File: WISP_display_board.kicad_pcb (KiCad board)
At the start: 2 copper layers, 261 x 160 mm, 109 parts, among them J1 Conn_01x09_Socket, U1 74HC595, U2 74HC595, U3 74HC595, U4 74HC595, U6 74HC595, U7 74HC595, U8 74HC595, U9 74HC595

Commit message: Full 15 rough draft
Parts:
- added Brd2: SSD1306, ssd1306_custom:128x64OLED, F.Cu at (-0.05, 53.3)
- added Brd3: SSD1306, ssd1306_custom:128x64OLED, F.Cu at (-0.05, 81.7)
- added Brd4: SSD1306, ssd1306_custom:128x64OLED, F.Cu at (-0.05, 110.2)
- added Brd5: SSD1306, ssd1306_custom:128x64OLED, F.Cu at (-0.05, 138.6)
- added Brd6: SSD1306, ssd1306_custom:128x64OLED, F.Cu at (28.5, 53.3)
- added Brd7: SSD1306, ssd1306_custom:128x64OLED, F.Cu at (28.5, 81.7)
- added Brd8: SSD1306, ssd1306_custom:128x64OLED, F.Cu at (28.5, 110.2)
- added J1: Conn_01x10_Socket, Connector_PinHeader_2.54mm:PinHeader_1x10_P2.54mm_Vertical, F.Cu at (45.4, 57.0)
- added R61: 4.7k, Resistor_SMD:R_0805_2012Metric_Pad1.20x1.40mm_HandSolder, F.Cu at (59.5, 62.1)
- added R62: 4.7k, Resistor_SMD:R_0805_2012Metric_Pad1.20x1.40mm_HandSolder, F.Cu at (59.5, 65.1)
- added R63: 4.7k, Resistor_SMD:R_0805_2012Metric_Pad1.20x1.40mm_HandSolder, F.Cu at (59.5, 68.0)
- added R64: 4.7k, Resistor_SMD:R_0805_2012Metric_Pad1.20x1.40mm_HandSolder, F.Cu at (59.5, 71.0)
- added R65: 4.7k, Resistor_SMD:R_0805_2012Metric_Pad1.20x1.40mm_HandSolder, F.Cu at (59.5, 73.9)
- added R66: 4.7k, Resistor_SMD:R_0805_2012Metric_Pad1.20x1.40mm_HandSolder, F.Cu at (59.5, 76.9)
- added R67: 4.7k, Resistor_SMD:R_0805_2012Metric_Pad1.20x1.40mm_HandSolder, F.Cu at (59.5, 79.8)
- added R68: 4.7k, Resistor_SMD:R_0805_2012Metric_Pad1.20x1.40mm_HandSolder, F.Cu at (64.3, 56.2)
- added R69: 4.7k, Resistor_SMD:R_0805_2012Metric_Pad1.20x1.40mm_HandSolder, F.Cu at (64.3, 59.2)
- added R70: 4.7k, Resistor_SMD:R_0805_2012Metric_Pad1.20x1.40mm_HandSolder, F.Cu at (64.3, 62.1)
- added R71: 4.7k, Resistor_SMD:R_0805_2012Metric_Pad1.20x1.40mm_HandSolder, F.Cu at (64.3, 65.1)
- added R72: 4.7k, Resistor_SMD:R_0805_2012Metric_Pad1.20x1.40mm_HandSolder, F.Cu at (64.3, 68.0)
- added R73: 4.7k, Resistor_SMD:R_0805_2012Metric_Pad1.20x1.40mm_HandSolder, F.Cu at (64.3, 71.0)
- added R74: 4.7k, Resistor_SMD:R_0805_2012Metric_Pad1.20x1.40mm_HandSolder, F.Cu at (64.3, 73.9)
- added R75: 4.7k, Resistor_SMD:R_0805_2012Metric_Pad1.20x1.40mm_HandSolder, F.Cu at (64.3, 76.9)
- added R76: 4.7k, Resistor_SMD:R_0805_2012Metric_Pad1.20x1.40mm_HandSolder, F.Cu at (64.3, 79.8)
- added U5: TCA9548APWR, Package_SO:TSSOP-24_4.4x7.8mm_P0.65mm, F.Cu at (71.5, 86.9)
- moved R23 197.5 mm to (50.0, 76.9), turned to 0 degrees
- moved R22 193.1 mm to (50.0, 73.9), turned to 0 degrees
- moved D10 192.1 mm to (49.0, 85.4)
- moved D11 192.1 mm to (53.0, 85.4)
- moved D9 192.1 mm to (45.0, 85.4)
- moved D12 192.1 mm to (56.9, 85.4)
- moved R21 188.9 mm to (50.0, 71.0), turned to 0 degrees
- moved R20 184.7 mm to (50.0, 68.0), turned to 0 degrees
- moved R19 180.6 mm to (50.0, 65.1), turned to 0 degrees
- moved R18 176.4 mm to (50.0, 62.1), turned to 0 degrees
- moved R17 172.2 mm to (50.0, 59.2), turned to 0 degrees
- moved R16 168.1 mm to (50.0, 56.2), turned to 0 degrees
- moved C7 155.3 mm to (78.1, 85.9)
- moved C3 153.3 mm to (78.1, 83.4)
- moved D29 152.4 mm to (53.0, 91.7)
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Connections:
- Brd1 pad 3: /I2C1_SCL -> /SC0
- Brd1 pad 4: /I2C1_SDA -> /SD0

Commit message: V1 routing
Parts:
- removed the Brd2 at (-0.05, 53.3)
- removed the Brd2 at (159.6, 147.7)
- removed C6, C7, C8: 0.1uF, Capacitor_SMD:C_0603_1608Metric_Pad1.08x0.95mm_HandSolder
- removed D21, D22, D23, D24, D25, D26, D27, D28, D29, D30: LED_Dual_AAKK, LED_SMD:LED_Kingbright_KPBD-3224
- removed the J1 at (101.2, 140.4)
- removed the J1 at (45.4, 57.0)
- removed R57, R58, R59, R60: 750, Resistor_SMD:R_0805_2012Metric_Pad1.20x1.40mm_HandSolder
- removed R61, R62, R63, R64, R65, R66, R67, R68, R69, R70, R71, R72, R73, R74, R75, R76: 4.7k, Resistor_SMD:R_0805_2012Metric_Pad1.20x1.40mm_HandSolder
- removed the U2 at (122.0, 183.9)
- removed the U3 at (49.5, 47.6)
- removed the U5 at (71.5, 86.9)
- removed U8: 74HC595, Package_SO:SOIC-16W_7.5x12.8mm_P1.27mm
- added Brd2: SSD1306, ssd1306_custom:128x64OLED, F.Cu at (339.0, 141.0)
- added J1: Conn_01x10_Socket, Connector_JST:JST_XH_B10B-XH-A_1x10_P2.50mm_Vertical, F.Cu at (147.2, 203.0)
- added U1: TCA9548APWR, Package_SO:TSSOP-24_4.4x7.8mm_P0.65mm, F.Cu at (158.1, 166.0)
- R17, R18, R19, R20, R21, R22, R23, R24, R41, R42, R43, R44, R45, R46, R47, R48: value 750 -> 4.7k
- moved R18 306.9 mm to (350.0, 126.9), turned to 180 degrees
- moved U4 303.0 mm to (325.9, 197.3), turned to 180 degrees
- moved R16 301.4 mm to (350.5, 80.0)
- moved R22 300.2 mm to (345.5, 126.9)
- moved D11 281.7 mm to (324.0, 162.0), turned to -90 degrees
- moved D12 279.9 mm to (323.9, 169.2), turned to -90 degrees
- moved R53 276.9 mm to (295.5, 201.9)
- moved R54 274.0 mm to (295.5, 199.0)
- moved R55 271.3 mm to (295.5, 196.1)
- moved C3 269.4 mm to (326.1, 188.4), turned to 180 degrees
- moved R56 268.6 mm to (295.5, 193.1)
- moved R52 260.5 mm to (274.5, 202.1), turned to 180 degrees
- moved R50 260.4 mm to (274.5, 196.1), turned to 180 degrees
- moved R51 260.4 mm to (274.5, 199.0), turned to 180 degrees
- moved Brd4 254.0 mm to (253.2, 91.2)
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- renumbered U6 to U2, U7 to U3, U9 to U5, U1 to U6
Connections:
- R10 pad 1: /LED6_G -> /LED5_R
- R10 pad 2: Net-(D6-A1) -> Net-(D5-A2)
- R11 pad 1: /LED6_R -> /LED6_G
- R11 pad 2: Net-(D6-A2) -> Net-(D6-A1)
- R12 pad 1: /LED7_G -> /LED6_R
- R12 pad 2: Net-(D7-A1) -> Net-(D6-A2)
- R13 pad 1: /LED7_R -> /LED7_G
- R13 pad 2: Net-(D7-A2) -> Net-(D7-A1)
- R14 pad 1: /LED8_G -> /LED7_R
- R14 pad 2: Net-(D8-A1) -> Net-(D7-A2)
- R15 pad 1: /LED8_R -> /LED8_G
- R15 pad 2: Net-(D8-A2) -> Net-(D8-A1)
- R16 pad 1: /LED9_G -> /LED8_R
- R16 pad 2: Net-(D9-A1) -> Net-(D8-A2)
- R17 pad 1: /LED9_R -> /SD0
- R17 pad 2: Net-(D9-A2) -> +3.3V
- R18 pad 1: /LED10_G -> /SD1
- R18 pad 2: Net-(D10-A1) -> +3.3V
- R19 pad 1: /LED10_R -> /SD2
- R19 pad 2: Net-(D10-A2) -> +3.3V
- R2 pad 1: /LED2_G -> /LED1_R
- R2 pad 2: Net-(D2-A1) -> Net-(D1-A2)
- R20 pad 1: /LED11_G -> /SD3
- R20 pad 2: Net-(D11-A1) -> +3.3V
- R21 pad 1: /LED11_R -> +3.3V
- R21 pad 2: Net-(D11-A2) -> /SC0
- R22 pad 1: /LED12_G -> +3.3V
- R22 pad 2: Net-(D12-A1) -> /SC1
- R23 pad 1: /LED12_R -> +3.3V
- R23 pad 2: Net-(D12-A2) -> /SC2
- R24 pad 1: /LED13_G -> +3.3V
- R24 pad 2: Net-(D13-A1) -> /SC3
- R25 pad 1: /LED13_R -> /LED9_G
- R25 pad 2: Net-(D13-A2) -> Net-(D9-A1)
- R26 pad 1: /LED14_G -> /LED9_R
- R26 pad 2: Net-(D14-A1) -> Net-(D9-A2)
- R27 pad 1: /LED14_R -> /LED10_G
- R27 pad 2: Net-(D14-A2) -> Net-(D10-A1)
- R28 pad 1: /LED15_G -> /LED10_R
- R28 pad 2: Net-(D15-A1) -> Net-(D10-A2)
- R29 pad 1: /LED15_R -> /LED11_G
- R29 pad 2: Net-(D15-A2) -> Net-(D11-A1)
- R3 pad 1: /LED2_R -> /LED2_G
- R3 pad 2: Net-(D2-A2) -> Net-(D2-A1)
- R30 pad 1: /LED16_G -> /LED11_R
- R30 pad 2: Net-(D16-A1) -> Net-(D11-A2)
- R31 pad 1: /LED16_R -> /LED12_G
- R31 pad 2: Net-(D16-A2) -> Net-(D12-A1)
- R32 pad 1: /LED1_R -> /LED12_R
- R32 pad 2: Net-(D1-A2) -> Net-(D12-A2)
- R33 pad 1: /LED17_G -> /LED13_G
- R33 pad 2: Net-(D17-A1) -> Net-(D13-A1)
- R34 pad 1: /LED17_R -> /LED13_R
- R34 pad 2: Net-(D17-A2) -> Net-(D13-A2)
- R35 pad 1: /LED18_G -> /LED14_G
- R35 pad 2: Net-(D18-A1) -> Net-(D14-A1)
- R36 pad 1: /LED18_R -> /LED14_R
- R36 pad 2: Net-(D18-A2) -> Net-(D14-A2)
- R37 pad 1: /LED19_G -> /LED15_G
- R37 pad 2: Net-(D19-A1) -> Net-(D15-A1)
- R38 pad 1: /LED19_R -> /LED15_R
- R38 pad 2: Net-(D19-A2) -> Net-(D15-A2)
- R39 pad 1: /LED20_G -> /LED16_G
- R39 pad 2: Net-(D20-A1) -> Net-(D16-A1)
- R4 pad 1: /LED3_G -> /LED2_R
- R4 pad 2: Net-(D3-A1) -> Net-(D2-A2)
- R40 pad 1: /LED20_R -> /LED16_R
- R40 pad 2: Net-(D20-A2) -> Net-(D16-A2)
- R41 pad 1: /LED21_G -> /SD4
- R41 pad 2: Net-(D21-A1) -> +3.3V
- R42 pad 1: /LED21_R -> /SD5
- R42 pad 2: Net-(D21-A2) -> +3.3V
- R43 pad 1: /LED22_G -> /SD6
- R43 pad 2: Net-(D22-A1) -> +3.3V
- R44 pad 1: /LED22_R -> /SD7
- R44 pad 2: Net-(D22-A2) -> +3.3V
- R45 pad 1: /LED23_G -> +3.3V
- R45 pad 2: Net-(D23-A1) -> /SC4
- R46 pad 1: /LED23_R -> +3.3V
- R46 pad 2: Net-(D23-A2) -> /SC5
- R47 pad 1: /LED24_G -> +3.3V
- R47 pad 2: Net-(D24-A1) -> /SC6
- R48 pad 1: /LED24_R -> +3.3V
- R48 pad 2: Net-(D24-A2) -> /SC7
- R49 pad 1: /LED25_G -> /LED17_G
- R49 pad 2: Net-(D25-A1) -> Net-(D17-A1)
- R5 pad 1: /LED3_R -> /LED3_G
- R5 pad 2: Net-(D3-A2) -> Net-(D3-A1)
- R50 pad 1: /LED25_R -> /LED17_R
- R50 pad 2: Net-(D25-A2) -> Net-(D17-A2)
- R51 pad 1: /LED26_G -> /LED18_G
- R51 pad 2: Net-(D26-A1) -> Net-(D18-A1)
- R52 pad 1: /LED26_R -> /LED18_R
- R52 pad 2: Net-(D26-A2) -> Net-(D18-A2)
- R53 pad 1: /LED27_G -> /LED19_G
- R53 pad 2: Net-(D27-A1) -> Net-(D19-A1)
- R54 pad 1: /LED27_R -> /LED19_R
- R54 pad 2: Net-(D27-A2) -> Net-(D19-A2)
- R55 pad 1: /LED28_G -> /LED20_G
- R55 pad 2: Net-(D28-A1) -> Net-(D20-A1)
- R56 pad 1: /LED28_R -> /LED20_R
- R56 pad 2: Net-(D28-A2) -> Net-(D20-A2)
- R6 pad 1: /LED4_G -> /LED3_R
- R6 pad 2: Net-(D4-A1) -> Net-(D3-A2)
- R7 pad 1: /LED4_R -> /LED4_G
- R7 pad 2: Net-(D4-A2) -> Net-(D4-A1)
- R8 pad 1: /LED5_G -> /LED4_R
- R8 pad 2: Net-(D5-A1) -> Net-(D4-A2)
- R9 pad 1: /LED5_R -> /LED5_G
- R9 pad 2: Net-(D5-A2) -> Net-(D5-A1)
- U4 pad 1: /LED29_R -> /LED9_R
- U4 pad 14: /SER_OUT7 -> /SER_OUT2
- U4 pad 15: /LED29_G -> /LED9_G
- U4 pad 2: /LED30_G -> /LED10_G
- U4 pad 3: /LED30_R -> /LED10_R
- U4 pad 4: unconnected-(U4-QE-Pad4) -> /LED11_G
- U4 pad 5: unconnected-(U4-QF-Pad5) -> /LED11_R
- U4 pad 6: unconnected-(U4-QG-Pad6) -> /LED12_G
- U4 pad 7: unconnected-(U4-QH-Pad7) -> /LED12_R
- U4 pad 9: unconnected-(U4-QH&apos;-Pad9) -> /SER_OUT3
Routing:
- net /SPI3_SCK: track 0.00 -> 466.0 mm, vias 0 -> 8
- net /SPI3_STCP: track 0.00 -> 462.3 mm, vias 0 -> 8
- net +3.3V: track 0.00 -> 335.9 mm, vias 0 -> 7
- net GND: track 0.00 -> 326.5 mm, vias 0 -> 23
- net /SD1: track 0.00 -> 206.5 mm, vias 0 -> 1
- net /SC1: track 0.00 -> 201.9 mm, vias 0 -> 1
- net /SER_OUT3: track 0.00 -> 192.3 mm, vias 0 -> 2
- net /SPI3_MOSI: track 0.00 -> 189.5 mm, vias 0 -> 2
- net /SER_OUT4: track 0.00 -> 155.3 mm, vias 0 -> 2
- net /SD3: track 0.00 -> 147.5 mm, vias 0 -> 1
- net /SC7: track 0.00 -> 144.1 mm, vias 0 -> 1
- net /SC3: track 0.00 -> 142.6 mm, vias 0 -> 1
- net /SD7: track 0.00 -> 138.5 mm, vias 0 -> 1
- net /SER_OUT2: track 0.00 -> 137.0 mm, vias 0 -> 2
- net Net-(D13-A2): track 0.00 -> 121.2 mm
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- added copper zone on In2.Cu, net +3.3V
- added copper zone on In1.Cu, net GND
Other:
- board size 261 x 160 mm -> 220 x 160 mm
- copper layers 2 -> 4

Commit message: Rough draft V2
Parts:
- C1, C2, C3, C4, C5: footprint Capacitor_SMD:C_0603_1608Metric_Pad1.08x0.95mm_HandSolder -> Capacitor_SMD:C_0805_2012Metric_Pad1.18x1.45mm_HandSolder
- J1: footprint Connector_JST:JST_XH_B10B-XH-A_1x10_P2.50mm_Vertical -> Connector_PinSocket_2.54mm:PinSocket_1x10_P2.54mm_Vertical
- moved C5 1.68 mm to (286.5, 189.0)
- moved C1 1.12 mm to (273.0, 53.0)
- moved C2 1.12 mm to (340.5, 77.5)
- moved C4 1.06 mm to (196.5, 81.0)
- moved C3 0.87 mm to (327.0, 188.5)
- moved J1 0.13 mm to (147.4, 203.0), turned to 90 degrees
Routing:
- net GND: track 326.5 -> 321.7 mm
- net +3.3V: track 335.9 -> 331.8 mm
- net /I2C1_SCL: track 50.4 -> 49.8 mm
- net /I2C_A1: track 40.0 -> 40.1 mm, vias 1 -> 2
- net /I2C_A2: track 40.0 -> 40.1 mm, vias 2 -> 1
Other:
- board text added: "3.3V"

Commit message: John revisions 9/7
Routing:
- added copper zone on B.Cu, net GND
- added copper zone on F.Cu, net GND
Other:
- board text added: "TCA"
- board text removed: "ECU"
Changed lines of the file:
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@@
 		)
 	)
-	(gr_text "ECU"
+	(gr_text "TCA"
 		(at 325 125.15 0)
 		(layer "F.SilkS")
@@
 	)
 	(gr_text "LOX"
-		(at 234.5 75.5 0)
+		(at 238.75 75.5 0)
 		(layer "F.SilkS")
 		(effects
@@
 	)
 	(zone
+		(net 3)
+		(net_name "GND")
+		(layer "F.Cu")
+		(hatch edge 0.5)
+		(priority 2)
+		(connect_pads
+			(clearance 0.5)
+		)
+		(min_thickness 0.25)
+		(filled_areas_thickness no)
+		(fill yes
+			(thermal_gap 0.5)
+			(thermal_bridge_width 0.5)
+		)
+		(polygon
+			(pts
+				(xy 137.5 50) (xy 137.5 210) (xy 357.5 210) (xy 357.5 50)
+			)
+		)
+	)
+	(zone
+		(net 3)
+		(net_name "GND")
+		(layer "B.Cu")
+		(hatch edge 0.5)
+		(priority 3)
+		(connect_pads
+			(clearance 0.5)
+		)
+		(min_thickness 0.25)
+		(filled_areas_thickness no)
+		(fill yes
+			(thermal_gap 0.5)
+			(thermal_bridge_width 0.5)
+		)
+		(polygon
+			(pts
+				(xy 137.5 50) (xy 137.5 210) (xy 357.5 210) (xy 357.5 50)
+			)
+		)
+	)
+	(zone

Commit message: Rough Draft V3
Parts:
- removed Brd8: SSD1306, ssd1306_custom:128x64OLED
- removed R44, R48: 4.7k, Resistor_SMD:R_0805_2012Metric_Pad1.20x1.40mm_HandSolder
- added H1: MountingHole, MountingHole:MountingHole_3.2mm_M3, F.Cu at (354.0, 53.5)
- added H2: MountingHole, MountingHole:MountingHole_3.2mm_M3, F.Cu at (354.0, 206.5)
- added H3: MountingHole, MountingHole:MountingHole_3.2mm_M3, F.Cu at (141.0, 206.5)
- added H4: MountingHole, MountingHole:MountingHole_3.2mm_M3, F.Cu at (141.0, 53.5)
- moved Brd7 17.8 mm to (157.1, 73.4)
- moved R43 17.8 mm to (174.1, 69.7)
- moved R47 17.8 mm to (174.1, 74.7)
- moved R42 9.90 mm to (173.9, 104.1)
- moved R46 9.90 mm to (173.9, 109.1)
- moved Brd6 9.90 mm to (157.0, 108.8)
- moved U1 7.63 mm to (158.0, 173.6)
- moved Brd5 2.38 mm to (157.0, 143.7)
- moved R41 2.38 mm to (174.5, 140.6)
- moved R45 2.38 mm to (174.5, 145.6)
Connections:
- U1 pad 19: /SD7 -> unconnected-(U1-SD7-Pad19)
- U1 pad 20: /SC7 -> unconnected-(U1-SC7-Pad20)
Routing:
- net /SC7: track 144.1 -> 0.00 mm, vias 1 -> 0
- net /SD7: track 138.5 -> 0.00 mm, vias 1 -> 0
- net +3.3V: track 331.8 -> 297.6 mm, vias 7 -> 14
- net /SD6: track 107.6 -> 133.2 mm
- net /SC6: track 112.5 -> 137.9 mm
- net /SD5: track 77.2 -> 95.0 mm
- net /SC5: track 81.9 -> 99.7 mm
- net /SD4: track 48.3 -> 58.8 mm
- net /SC4: track 53.2 -> 63.6 mm
- net /I2C_A2: track 40.1 -> 31.7 mm
- net /SC3: track 142.6 -> 150.7 mm
- net /SD3: track 147.5 -> 155.4 mm
- net /SC2: track 72.0 -> 79.7 mm
- net /I2C_A0: track 38.2 -> 30.6 mm
- net /SD2: track 76.3 -> 83.9 mm
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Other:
- outline, holes or cut-outs redrawn

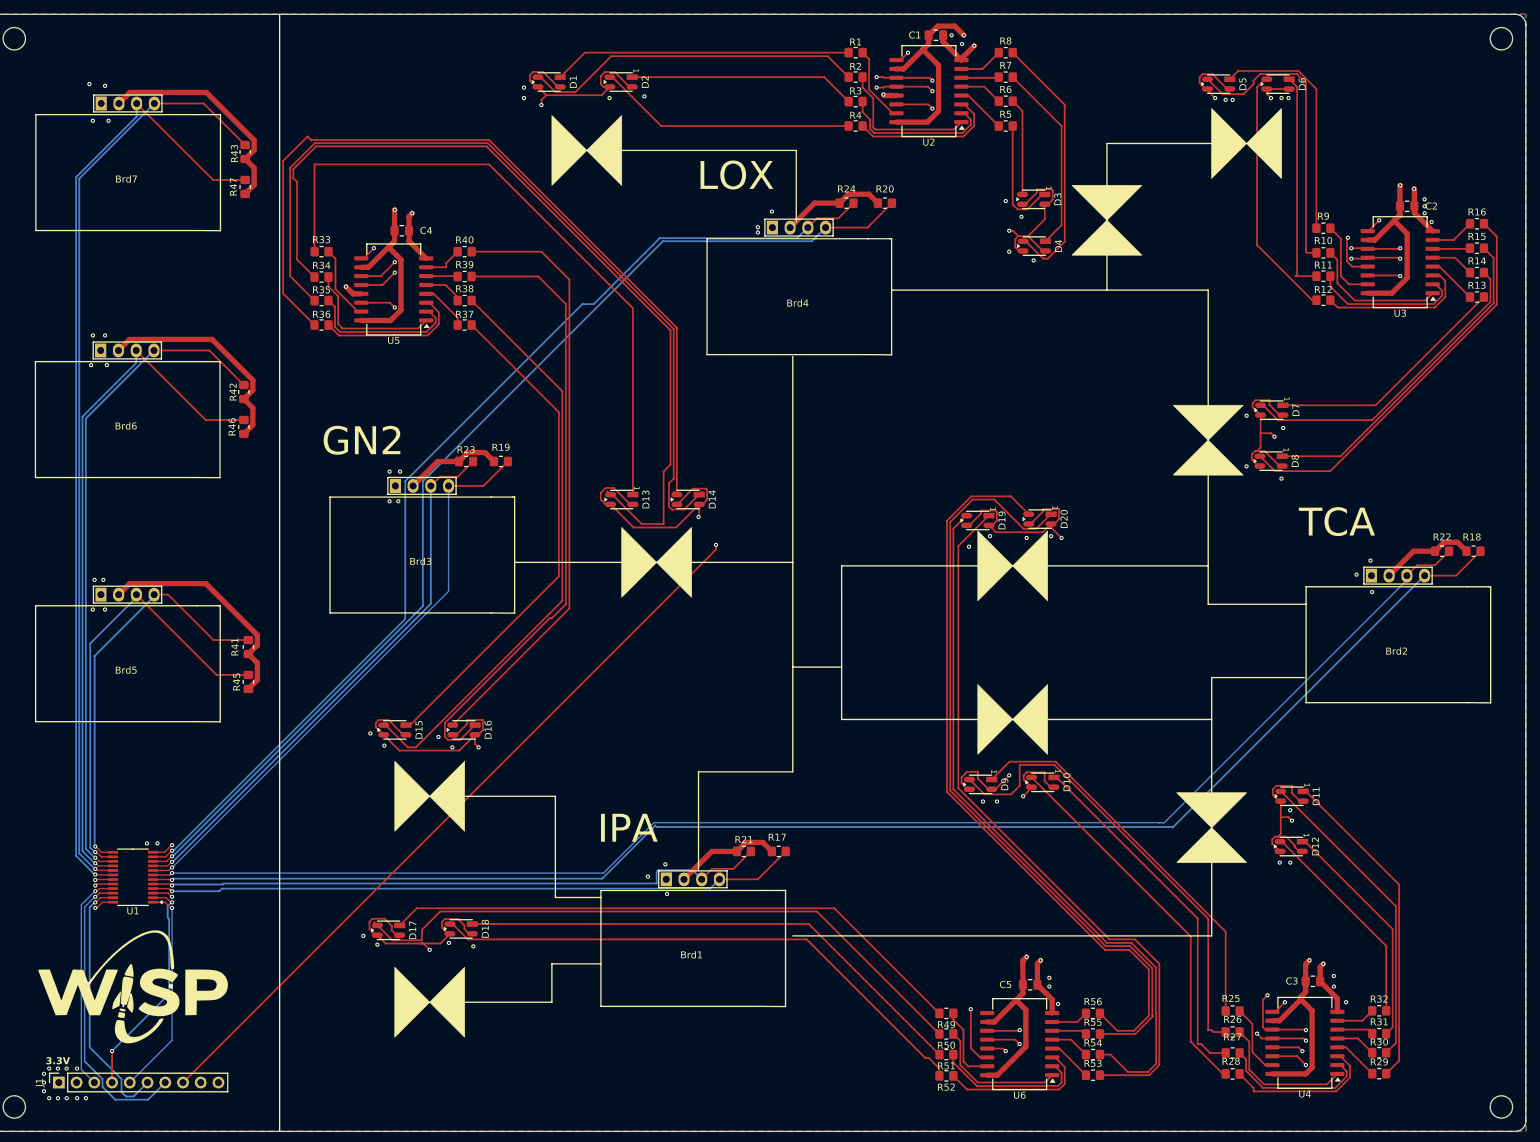
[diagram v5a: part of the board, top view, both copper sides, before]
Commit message: Fixed LED orientation
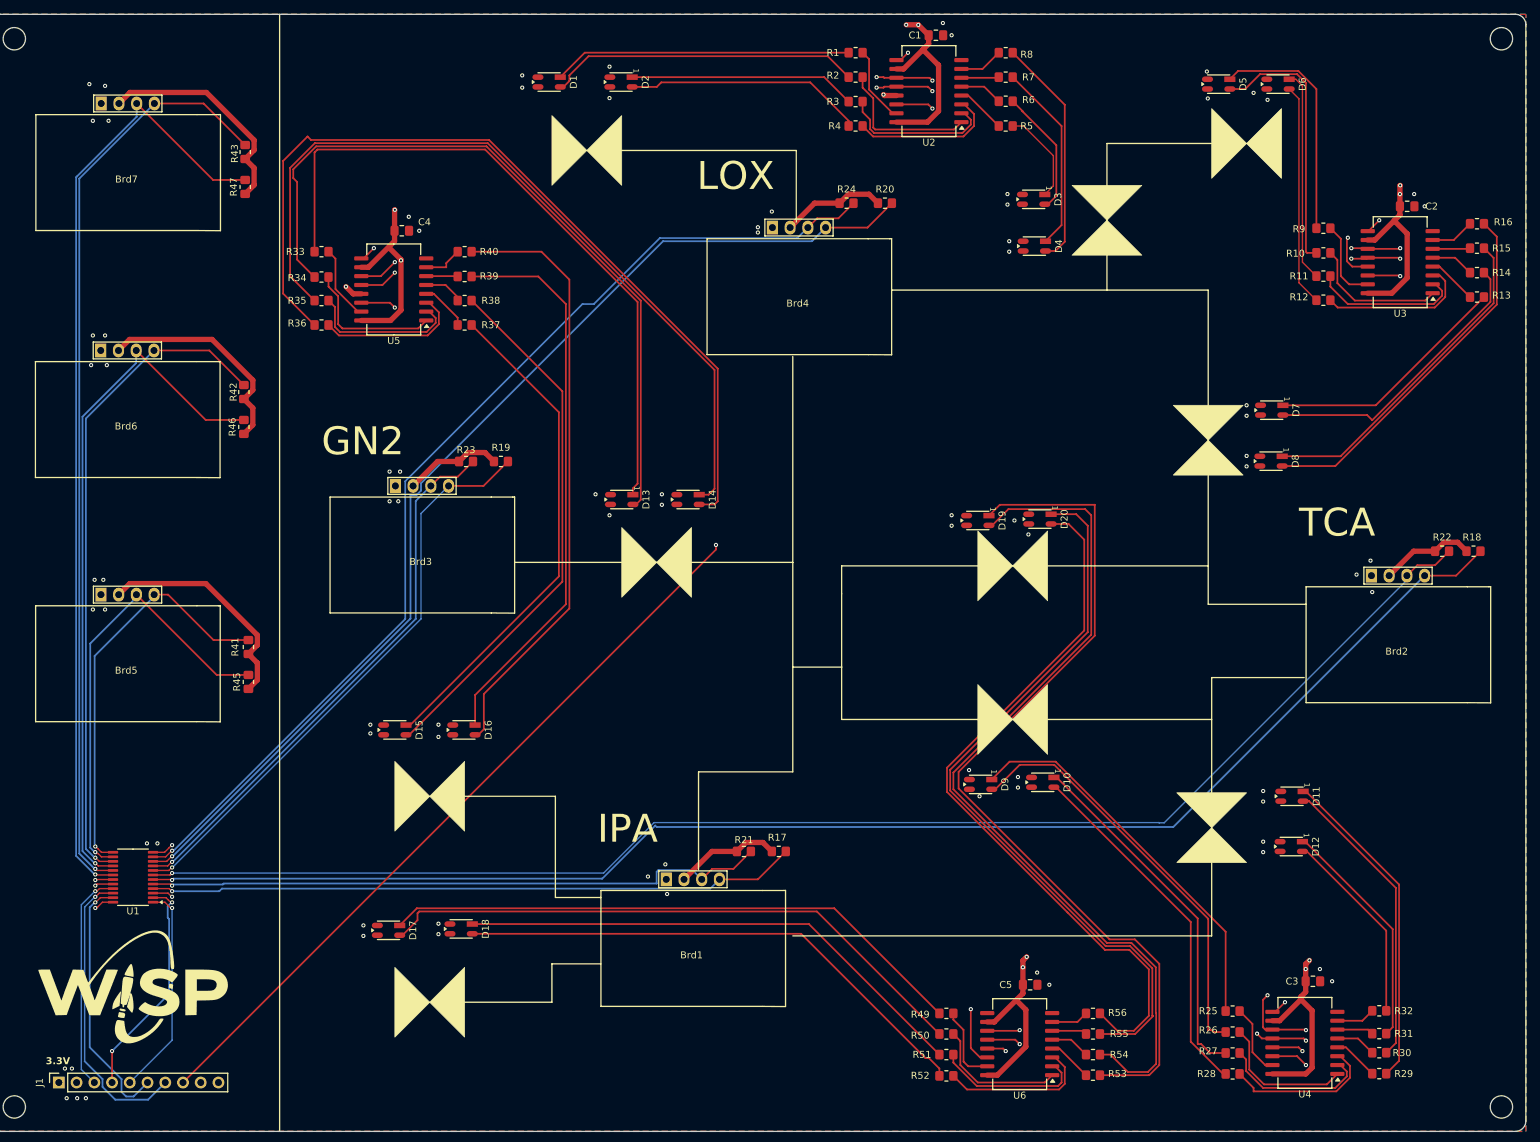
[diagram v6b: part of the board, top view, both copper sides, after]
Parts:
- D1, D10, D11, D12, D13, D14, D15, D16, D17, D18, D19, D2, D20, D3, D4, D5, D6, D7, D8, D9: value LED_Dual_AAKK -> LED_Dual_AKAK
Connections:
- D1 pad 2: Net-(D1-A2) -> GND
- D1 pad 3: GND -> Net-(D1-A2)
- D10 pad 2: Net-(D10-A2) -> GND
- D10 pad 3: GND -> Net-(D10-A2)
- D11 pad 2: Net-(D11-A2) -> GND
- D11 pad 3: GND -> Net-(D11-A2)
- D12 pad 2: Net-(D12-A2) -> GND
- D12 pad 3: GND -> Net-(D12-A2)
- D13 pad 2: Net-(D13-A2) -> GND
- D13 pad 3: GND -> Net-(D13-A2)
- D14 pad 2: Net-(D14-A2) -> GND
- D14 pad 3: GND -> Net-(D14-A2)
- D15 pad 2: Net-(D15-A2) -> GND
- D15 pad 3: GND -> Net-(D15-A2)
- D16 pad 2: Net-(D16-A2) -> GND
- D16 pad 3: GND -> Net-(D16-A2)
- D17 pad 2: Net-(D17-A2) -> GND
- D17 pad 3: GND -> Net-(D17-A2)
- D18 pad 2: Net-(D18-A2) -> GND
- D18 pad 3: GND -> Net-(D18-A2)
- D19 pad 2: Net-(D19-A2) -> GND
- D19 pad 3: GND -> Net-(D19-A2)
- D2 pad 2: Net-(D2-A2) -> GND
- D2 pad 3: GND -> Net-(D2-A2)
- D20 pad 2: Net-(D20-A2) -> GND
- D20 pad 3: GND -> Net-(D20-A2)
- D3 pad 2: Net-(D3-A2) -> GND
- D3 pad 3: GND -> Net-(D3-A2)
- D4 pad 2: Net-(D4-A2) -> GND
- D4 pad 3: GND -> Net-(D4-A2)
- D5 pad 2: Net-(D5-A2) -> GND
- D5 pad 3: GND -> Net-(D5-A2)
- D6 pad 2: Net-(D6-A2) -> GND
- D6 pad 3: GND -> Net-(D6-A2)
- D7 pad 2: Net-(D7-A2) -> GND
- D7 pad 3: GND -> Net-(D7-A2)
- D8 pad 2: Net-(D8-A2) -> GND
- D8 pad 3: GND -> Net-(D8-A2)
- D9 pad 2: Net-(D9-A2) -> GND
- D9 pad 3: GND -> Net-(D9-A2)
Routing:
- net GND: track 321.1 -> 29.3 mm, vias 100 -> 88
- net Net-(D19-A1): track 103.7 -> 127.3 mm
- net Net-(D19-A2): track 103.0 -> 126.4 mm
- net Net-(D13-A2): track 121.2 -> 107.3 mm
- net Net-(D16-A1): track 89.9 -> 80.9 mm
- net Net-(D15-A2): track 84.2 -> 77.5 mm
- net +3.3V: track 297.6 -> 303.3 mm, vias 14 -> 12
- net Net-(D9-A2): track 66.3 -> 60.6 mm
- net Net-(D14-A2): track 119.1 -> 124.7 mm
- net Net-(D17-A2): track 91.9 -> 87.0 mm
- net Net-(D20-A1): track 111.9 -> 107.1 mm
- net Net-(D6-A2): track 36.3 -> 31.9 mm
- net Net-(D3-A2): track 13.9 -> 18.3 mm
- net Net-(D1-A2): track 49.2 -> 44.8 mm
- net Net-(D4-A2): track 38.2 -> 33.8 mm
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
